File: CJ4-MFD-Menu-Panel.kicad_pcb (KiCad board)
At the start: 2 copper layers, 145.3 x 65.8 mm, 51 parts, among them J1 Conn_02x06_Counter_Clockwise, SW1 SW_Push_LED, SW10 5_Way_Switch, SW11 SW_Push_LED, SW12 SW_Push_LED, SW13 SW_Push_LED, SW14 SW_Push_LED, SW15 SW_Push_LED, SW16 SW_Push_LED, SW17 SW_Push_LED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

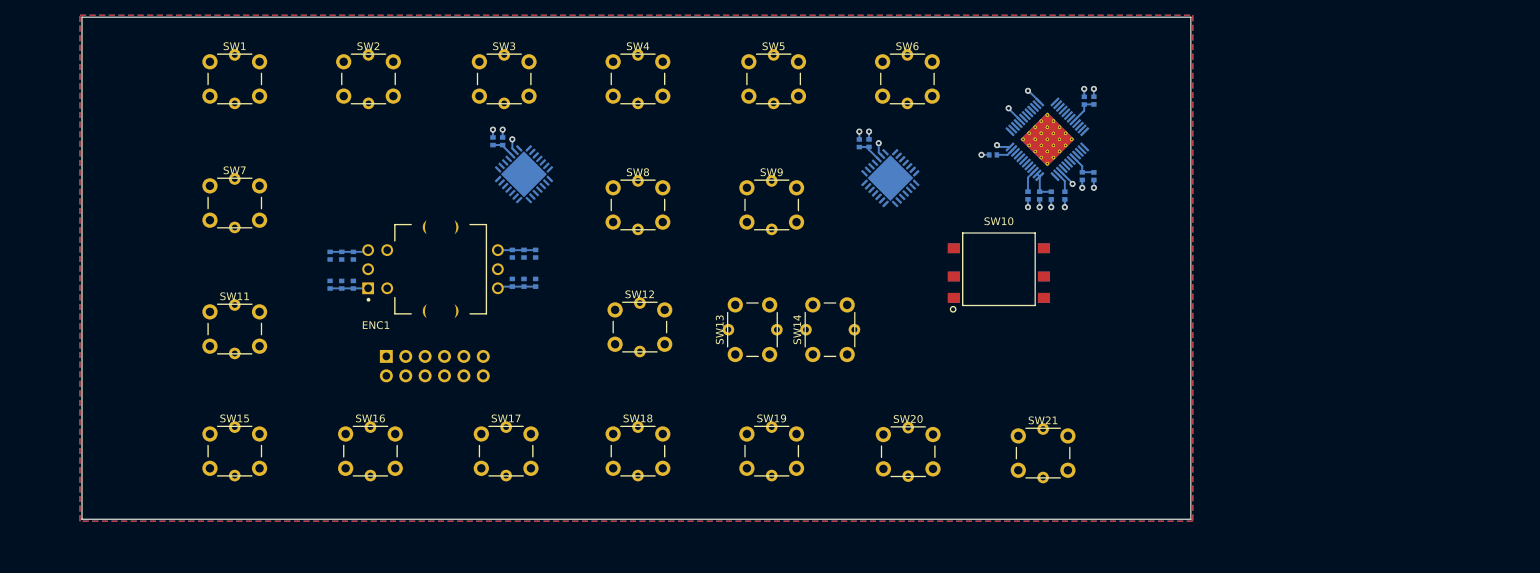
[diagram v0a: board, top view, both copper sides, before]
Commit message: Switch footprint, attempt routing
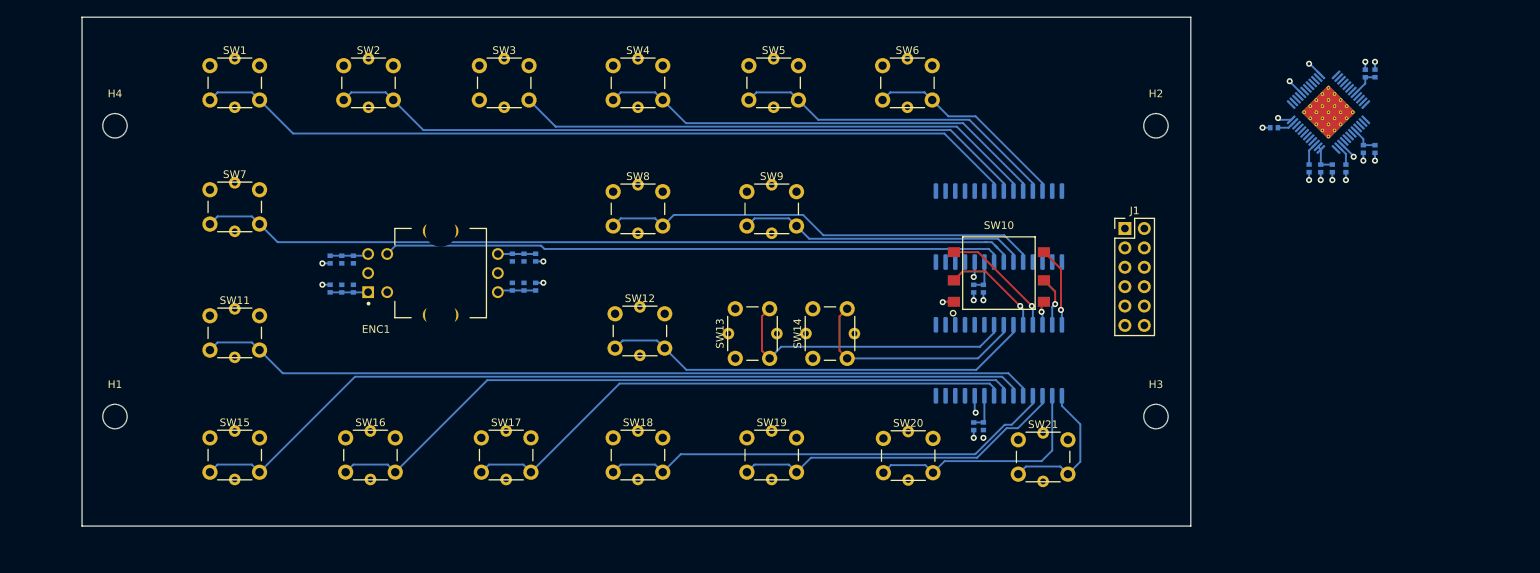
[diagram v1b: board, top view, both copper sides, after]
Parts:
- added H1: MountingHole, MountingHole:MountingHole_3.2mm_M3, F.Cu at (17.5, 65.3)
- added H2: MountingHole, MountingHole:MountingHole_3.2mm_M3, F.Cu at (153.9, 27.2)
- added H3: MountingHole, MountingHole:MountingHole_3.2mm_M3, F.Cu at (153.9, 65.3)
- added H4: MountingHole, MountingHole:MountingHole_3.2mm_M3, F.Cu at (17.5, 27.2)
- J1: moved to F.Cu
- U1, U2: value MCP23017_ML -> MCP23017_SO; footprint Package_DFN_QFN:QFN-28-1EP_6x6mm_P0.65mm_EP4.25x4.25mm -> Package_SO:SOIC-28W_7.5x17.9mm_P1.27mm
- moved J1 98.2 mm to (149.9, 40.6), turned to 0 degrees
- moved C6 67.1 mm to (131.3, 48.5), turned to 270 degrees
- moved C5 64.7 mm to (130.0, 48.5), turned to 270 degrees
- moved U1 62.6 mm to (133.3, 40.4), turned to 90 degrees
- moved C7 40.0 mm to (131.3, 66.5), turned to 270 degrees
- moved C8 40.0 mm to (130.0, 66.6), turned to 270 degrees
- moved C11 37.0 mm to (181.1, 30.2)
- moved C12 37.0 mm to (182.6, 30.2)
- moved C13 37.0 mm to (175.5, 32.8)
- moved C14 37.0 mm to (177.0, 32.8)
- moved C15 37.0 mm to (174.0, 32.8)
- moved C9 37.0 mm to (182.6, 20.3)
- moved R10 37.0 mm to (178.8, 32.8)
- moved U3 37.0 mm to (176.5, 25.4)
- moved C10 37.0 mm to (181.4, 20.3)
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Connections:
- U1 pad 1: ESC -> Net-(U1-Pad1)
- U1 pad 10: Net-(U1-Pad10) -> GND
- U1 pad 12: Net-(U1-Pad11) -> SCL
- U1 pad 13: Net-(U1-Pad11) -> SDA
- U1 pad 14: +5V -> Net-(U1-Pad14)
- U1 pad 16: INTA_1 -> Net-(U1-Pad15)
- U1 pad 17: NAV_DATA -> Net-(U1-Pad15)
- U1 pad 18: MEM_1 -> +5V
- U1 pad 19: MEM_2 -> Net-(U1-Pad19)
- U1 pad 2: TERR_WX -> Net-(U1-Pad2)
- U1 pad 20: MEM_3 -> INTA_1
- U1 pad 21: CHART -> UPR_MENU
- U1 pad 22: RADAR_MENU -> ESC
- U1 pad 23: ZOOM_MINUS -> DATABASE
- U1 pad 24: SYS -> NAV_DATA
- U1 pad 25: UPR_MENU -> CHART
- U1 pad 26: LWR_MENU -> CAS_PAGE
- U1 pad 27: CRSR -> Net-(U1-Pad27)
- U1 pad 28: ENG -> Net-(U1-Pad28)
- U1 pad 3: DATABASE -> Net-(U1-Pad3)
- U1 pad 4: TFC -> Net-(U1-Pad4)
- U1 pad 5: +5V -> MEM_1
- U1 pad 6: GND -> RADAR_MENU
- U1 pad 7: Net-(U1-Pad7) -> LWR_MENU
- U1 pad 8: SCL -> E_BTN
- U1 pad 9: SDA -> +5V
- U2 pad 1: LEFT -> PASS_BRIEF
- U2 pad 10: Net-(U2-Pad10) -> GND
- U2 pad 11: +5V -> Net-(U2-Pad11)
- U2 pad 12: Net-(U2-Pad12) -> SCL
- U2 pad 13: Net-(U2-Pad12) -> SDA
- U2 pad 14: +5V -> Net-(U2-Pad14)
- U2 pad 15: Net-(U2-Pad15) -> +5V
- U2 pad 16: INTA_2 -> Net-(U2-Pad16)
- U2 pad 17: DOWN -> Net-(U2-Pad16)
- U2 pad 18: E_BTN -> +5V
- U2 pad 2: CTR -> CKLIST
- U2 pad 20: Net-(U2-Pad20) -> INTA_2
- U2 pad 21: Net-(U2-Pad21) -> ZOOM_MINUS
- U2 pad 22: Net-(U2-Pad22) -> ZOOM_PLUS
- U2 pad 23: Net-(U2-Pad23) -> MEM_2
- U2 pad 24: Net-(U2-Pad24) -> LEFT
- U2 pad 25: CAS_PAGE -> CTR
- U2 pad 26: ZOOM_PLUS -> DOWN
- U2 pad 27: CKLIST -> RIGHT
- U2 pad 28: PASS_BRIEF -> UP
- U2 pad 3: UP -> SYS
- U2 pad 4: RIGHT -> MEM_3
- U2 pad 5: +5V -> CRSR
- U2 pad 6: GND -> ENG
- U2 pad 7: Net-(U2-Pad7) -> TERR_WX
- U2 pad 8: SCL -> TFC
- U2 pad 9: SDA -> +5V
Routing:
- net ENG: track 0.00 -> 112.9 mm
- net CRSR: track 0.00 -> 110.5 mm
- net UPR_MENU: track 0.00 -> 109.1 mm
- net LWR_MENU: track 0.00 -> 108.1 mm
- net TERR_WX: track 0.00 -> 93.5 mm
- net ESC: track 0.00 -> 92.9 mm
- net E_BTN: track 0.00 -> 81.5 mm
- net TFC: track 0.00 -> 74.1 mm
- net DATABASE: track 0.00 -> 69.0 mm
- net MEM_3: track 0.00 -> 60.6 mm
- net NAV_DATA: track 0.00 -> 60.1 mm
- net MEM_1: track 0.00 -> 58.3 mm
- net MEM_2: track 0.00 -> 57.2 mm
- net SYS: track 0.00 -> 44.3 mm
- net CHART: track 0.00 -> 43.6 mm
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- removed copper zone on B.Cu, net GND
- removed copper zone on F.Cu, net GND
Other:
- board size 145.3 x 65.8 mm -> 145.3 x 66.7 mm

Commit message: Footprint changes, update board size
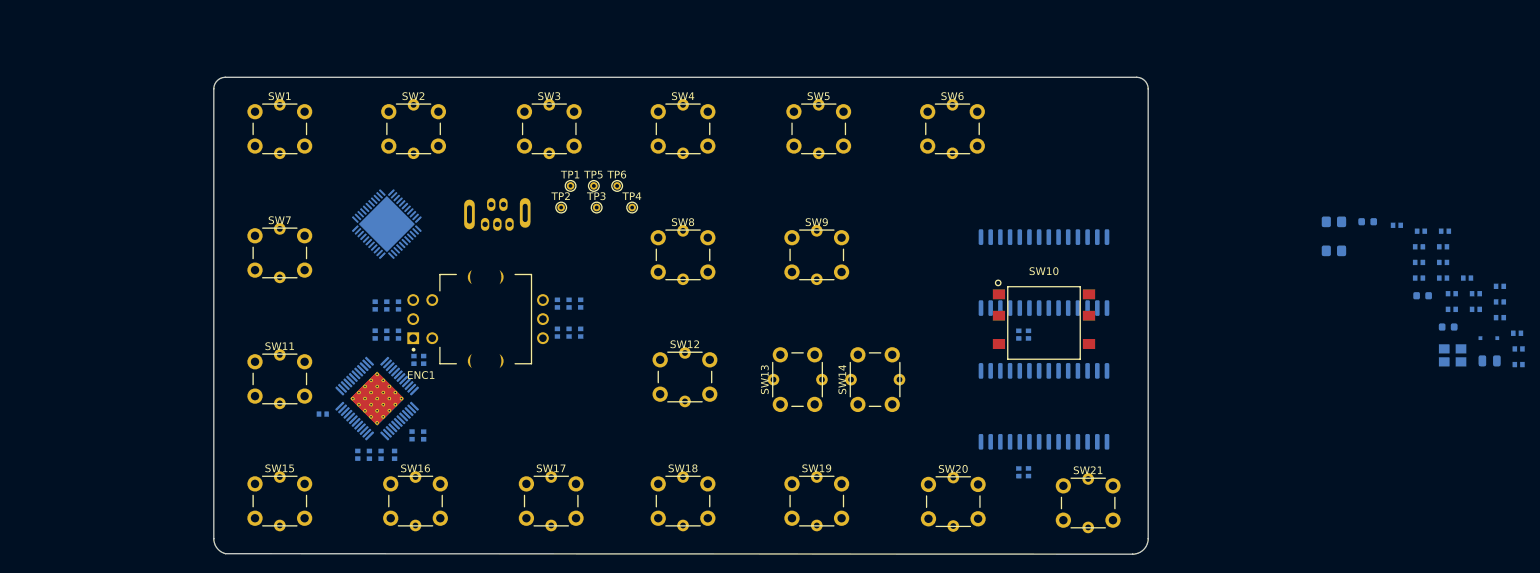
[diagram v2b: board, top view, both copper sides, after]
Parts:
- removed H1, H2, H3, H4: MountingHole, MountingHole:MountingHole_3.2mm_M3
- added C16: 10uF, Collins-FMS-3000:Perfect_0402, B.Cu at (201.2, 54.4)
- added C17: 100nf, Collins-FMS-3000:Perfect_0402, B.Cu at (188.4, 45.1)
- added C18: 100nf, Collins-FMS-3000:Perfect_0402, B.Cu at (188.4, 43.0)
- added C19: 100nf, Collins-FMS-3000:Perfect_0402, B.Cu at (191.5, 47.1)
- added C20: 100nf, Collins-FMS-3000:Perfect_0402, B.Cu at (201.4, 56.4)
- added C21: 10uF, Collins-FMS-3000:Perfect_0402, B.Cu at (195.8, 51.2)
- added C22: 1uF, Collins-FMS-3000:Perfect_0402, B.Cu at (185.5, 40.2)
- added C23: 100nf, Collins-FMS-3000:Perfect_0402, B.Cu at (188.4, 47.1)
- added C24: 100nf, Collins-FMS-3000:Perfect_0402, B.Cu at (192.7, 49.2)
- added C25: 1uF, Collins-FMS-3000:Perfect_0402, B.Cu at (192.7, 51.2)
- added C26: 20pF, Collins-FMS-3000:Perfect_0402, B.Cu at (201.4, 58.5)
- added C27: 20pF, Collins-FMS-3000:Perfect_0402, B.Cu at (191.5, 45.1)
- added D1: GREEN, Collins-FMS-3000:LED_0603_1608Metric, B.Cu at (192.2, 53.6)
- added D2: YELLOW, Collins-FMS-3000:LED_0603_1608Metric, B.Cu at (188.9, 49.5)
- added D3: D_Small, Diode_SMD:D_SOD-323F, B.Cu at (197.5, 55.0)
- added D4: GREEN, Collins-FMS-3000:LED_0603_1608Metric, B.Cu at (181.7, 39.8)
- added FB1: Ferrite_Bead_Small, Capacitor_SMD:C_0805_2012Metric, B.Cu at (197.6, 58.0)
- added R11: 1K, Collins-FMS-3000:Perfect_0402, B.Cu at (188.6, 41.0)
- added R12: 22, Collins-FMS-3000:Perfect_0402, B.Cu at (194.7, 47.1)
- added R13: 330, Collins-FMS-3000:Perfect_0402, B.Cu at (195.8, 49.2)
- added R14: 22, Collins-FMS-3000:Perfect_0402, B.Cu at (199.0, 48.2)
- added R15: 10k, Collins-FMS-3000:Perfect_0402, B.Cu at (191.8, 41.0)
- added R16: 2k, Resistor_SMD:R_0805_2012Metric_Pad1.20x1.40mm_HandSolder, B.Cu at (177.2, 43.6)
- added R17: 2k, Resistor_SMD:R_0805_2012Metric_Pad1.20x1.40mm_HandSolder, B.Cu at (177.2, 39.8)
- added R19: 100k, Collins-FMS-3000:Perfect_0402, B.Cu at (199.0, 50.3)
- added R20: 330, Collins-FMS-3000:Perfect_0402, B.Cu at (191.5, 43.0)
- added R21: 10k, Collins-FMS-3000:Perfect_0402, B.Cu at (199.0, 52.3)
- added TP1: TestPoint_Flag, TestPoint:TestPoint_THTPad_D1.0mm_Drill0.5mm, F.Cu at (77.2, 35.1)
- added TP2: TestPoint_Flag, TestPoint:TestPoint_THTPad_D1.0mm_Drill0.5mm, F.Cu at (76.0, 37.9)
- added TP3: TestPoint_Flag, TestPoint:TestPoint_THTPad_D1.0mm_Drill0.5mm, F.Cu at (80.6, 37.9)
- added TP4: TestPoint_Flag, TestPoint:TestPoint_THTPad_D1.0mm_Drill0.5mm, F.Cu at (85.3, 37.9)
- added TP5: TestPoint_Flag, TestPoint:TestPoint_THTPad_D1.0mm_Drill0.5mm, F.Cu at (80.3, 35.1)
- added TP6: TestPoint_Flag, TestPoint:TestPoint_THTPad_D1.0mm_Drill0.5mm, F.Cu at (83.3, 35.1)
- added U4: ATmega32U4RC-MU, Package_DFN_QFN:QFN-44-1EP_7x7mm_P0.5mm_EP5.2x5.2mm, B.Cu at (53.1, 40.1)
- added Y1: 16MHz, Crystal:Crystal_SMD_3225-4Pin_3.2x2.5mm, B.Cu at (192.8, 57.3)
- J1: value Conn_02x06_Counter_Clockwise -> USB_B_Mini; footprint Connector_PinHeader_2.54mm:PinHeader_2x06_P2.54mm_Vertical -> Collins-FMS-3000:USB_B_Mini_Amphenol_UE25BE5510H; moved to B.Cu
- moved C10 130.2 mm to (56.7, 57.9)
- moved C11 130.2 mm to (56.5, 67.7)
- moved C12 130.2 mm to (58.0, 67.8)
- moved C13 130.2 mm to (50.9, 70.3)
- moved C14 130.2 mm to (52.4, 70.3)
- moved C15 130.2 mm to (49.3, 70.3)
- moved C9 130.2 mm to (58.0, 57.8)
- moved R10 130.2 mm to (54.2, 70.3)
- moved R9 130.2 mm to (44.8, 65.0)
- moved U3 130.2 mm to (51.9, 62.9)
- moved J1 82.3 mm to (67.6, 38.8)
- moved SW21 8.44 mm to (141.8, 74.4)
- moved SW10 8.44 mm to (139.3, 52.8)
- moved U1 8.44 mm to (139.3, 46.4)
- moved U2 8.44 mm to (139.3, 63.9)
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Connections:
- J1 pad 1: +5V -> /ATmega32u4/VBUS
- J1 pad 2: SDA -> /ATmega32u4/DR-
- J1 pad 3: SCL -> /ATmega32u4/DR+
- J1 pad 4: INTA_1 -> Net-(J1-Pad4)
- J1 pad 5: INTA_2 -> GND
- J1 pad 6: SDB -> GND
- U1 pad 15: Net-(U1-Pad15) -> GND
- U1 pad 16: Net-(U1-Pad15) -> GND
- U1 pad 17: Net-(U1-Pad15) -> GND
- U2 pad 16: Net-(U2-Pad16) -> GND
- U2 pad 17: Net-(U2-Pad16) -> GND
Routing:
- net ENG: track 112.9 -> 0.00 mm
- net CRSR: track 110.5 -> 0.00 mm
- net UPR_MENU: track 109.1 -> 0.00 mm
- net LWR_MENU: track 108.1 -> 0.00 mm
- net TERR_WX: track 93.5 -> 0.00 mm
- net ESC: track 92.9 -> 0.00 mm
- net E_BTN: track 81.5 -> 0.00 mm
- net TFC: track 74.1 -> 0.00 mm
- net DATABASE: track 69.0 -> 0.00 mm
- net MEM_3: track 60.6 -> 0.00 mm
- net NAV_DATA: track 60.1 -> 0.00 mm
- net MEM_1: track 58.3 -> 0.00 mm
- net MEM_2: track 57.2 -> 0.00 mm
- net SYS: track 44.3 -> 0.00 mm
- net CHART: track 43.6 -> 0.00 mm
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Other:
- board size 145.3 x 66.7 mm -> 122.4 x 62.5 mm

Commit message: Switch to jtag
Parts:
- removed TP1, TP3, TP5, TP6: TestPoint_Flag, TestPoint:TestPoint_THTPad_D1.0mm_Drill0.5mm
- added J2: AVR-ISP-6, Connector:Tag-Connect_TC2030-IDC-NL_2x03_P1.27mm_Vertical, B.Cu at (77.2, 62.0)

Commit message: ATmega32u4 layout in progress
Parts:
- removed D2: YELLOW, Collins-FMS-3000:LED_0603_1608Metric
- removed D4: GREEN, Collins-FMS-3000:LED_0603_1608Metric
- removed R13, R20: 330, Collins-FMS-3000:Perfect_0402
- removed TP2, TP4: TestPoint_Flag, TestPoint:TestPoint_THTPad_D1.0mm_Drill0.5mm
- moved C20 183.1 mm to (18.3, 56.7)
- moved C23 183.1 mm to (5.26, 47.4)
- moved C24 183.1 mm to (9.56, 49.4)
- moved D3 183.1 mm to (14.4, 55.3)
- moved FB1 183.1 mm to (14.5, 58.2)
- moved R11 183.1 mm to (5.51, 41.2)
- moved R12 183.1 mm to (11.6, 47.4)
- moved R15 183.1 mm to (8.66, 41.2)
- moved C21 183.1 mm to (12.7, 51.5)
- moved D1 183.1 mm to (9.08, 53.8)
- moved R14 183.1 mm to (15.9, 48.5)
- moved R21 154.7 mm to (44.7, 41.7), turned to 90 degrees
- moved R19 154.4 mm to (44.7, 44.5), turned to 270 degrees
- moved C16 147.8 mm to (54.9, 34.0), turned to 90 degrees
- moved C26 145.8 mm to (56.1, 47.0), turned to 270 degrees
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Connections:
- R17 pad 1: +5V -> SDA
- R17 pad 2: SDA -> +5V
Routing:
- net +5V: track 0.00 -> 57.1 mm, vias 0 -> 9
- net GND: track 0.00 -> 22.9 mm, vias 0 -> 16
- net SDA: track 0.00 -> 18.7 mm, vias 0 -> 2
- net SCL: track 0.00 -> 17.3 mm, vias 0 -> 2
- net /ATmega32u4/XTAL2: track 0.00 -> 9.20 mm
- net SDB: track 0.00 -> 7.34 mm, vias 0 -> 2
- net /ATmega32u4/XTAL1: track 0.00 -> 6.81 mm
- net INTA_1: track 0.00 -> 5.68 mm, vias 0 -> 1
- net Net-(R21-Pad2): track 0.00 -> 4.52 mm, vias 0 -> 2
- net INTA_2: track 0.00 -> 3.71 mm, vias 0 -> 1
- net /ATmega32u4/D+: track 0.00 -> 3.09 mm
- net Net-(C25-Pad1): track 0.00 -> 3.01 mm
- net Net-(C22-Pad1): track 0.00 -> 2.77 mm
- net /ATmega32u4/D-: track 0.00 -> 2.70 mm
- net RESET: track 0.00 -> 2.53 mm
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
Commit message: More routing. What a pain.
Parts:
- moved D1 70.6 mm to (77.0, 34.3), turned to 270 degrees
- moved R11 70.3 mm to (75.4, 34.3), turned to 270 degrees
- moved C23 65.7 mm to (70.9, 43.2), turned to 180 degrees
- moved C21 63.8 mm to (74.2, 34.3), turned to 270 degrees
- moved FB1 62.2 mm to (72.1, 34.8), turned to 270 degrees
- moved R15 62.2 mm to (70.9, 40.6), turned to 180 degrees
- moved C24 61.8 mm to (70.9, 41.9), turned to 180 degrees
- moved D3 59.3 mm to (71.4, 38.9), turned to 180 degrees
- moved R12 49.7 mm to (59.2, 33.3)
- moved R14 46.3 mm to (59.2, 32.0)
- moved C20 43.4 mm to (59.2, 42.2)
- moved R19 13.7 mm to (34.5, 53.6), turned to 90 degrees
- moved C1 12.4 mm to (63.9, 49.8), turned to 90 degrees
- moved C3 12.3 mm to (63.9, 54.7), turned to 270 degrees
- moved J2 12.1 mm to (66.0, 40.6)
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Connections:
- U4 pad 1: LED_INTB -> INTA_2
- U4 pad 21: INTA_2 -> LED_INTB
- U4 pad 25: SDB -> Net-(U4-Pad25)
- U4 pad 27: Net-(U4-Pad27) -> SDB
- U4 pad 28: Net-(U4-Pad28) -> A
- U4 pad 29: Net-(U4-Pad29) -> A'
- U4 pad 30: Net-(U4-Pad30) -> B
- U4 pad 31: Net-(U4-Pad31) -> B'
- U4 pad 37: E_BTN -> Net-(U4-Pad37)
- U4 pad 38: B' -> Net-(U4-Pad38)
- U4 pad 39: A' -> Net-(U4-Pad39)
- U4 pad 40: B -> Net-(U4-Pad40)
- U4 pad 41: A -> Net-(U4-Pad41)
- U4 pad 44: +5V -> Net-(U4-Pad44)
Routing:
- net A: track 0.00 -> 44.9 mm, vias 0 -> 1
- net B: track 0.00 -> 43.3 mm, vias 0 -> 1
- net A': track 0.00 -> 30.8 mm, vias 0 -> 1
- net B': track 0.00 -> 28.6 mm, vias 0 -> 1
- net +5V: track 57.1 -> 83.5 mm, vias 9 -> 8
- net SDB: track 7.34 -> 32.2 mm
- net /ATmega32u4/MOSI: track 0.00 -> 11.5 mm, vias 0 -> 2
- net SDA: track 18.7 -> 29.7 mm
- net LED_INTB: track 2.43 -> 13.2 mm
- net /ATmega32u4/SCK: track 0.00 -> 10.4 mm
- net /ATmega32u4/DR+: track 0.00 -> 10.1 mm
- net /ATmega32u4/DR-: track 0.00 -> 8.01 mm
- net /ATmega32u4/MISO: track 0.00 -> 7.92 mm, vias 0 -> 2
- net INTA_1: track 5.68 -> 13.5 mm, vias 1 -> 0
- net GND: track 22.9 -> 30.3 mm, vias 16 -> 20
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- added copper zone on B.Cu, net GND
- added copper zone on F.Cu, net GND
